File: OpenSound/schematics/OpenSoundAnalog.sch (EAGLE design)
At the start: 68 parts, among them IC1 MCP4822-E/PSOIC8, IC2 QUAD_OPAMPD, IC3 LM317MABT, Q601 BC846, Q701 BC846, Q801 BC846, Q903 BC846, U1 SN74LVC3G17DCTR

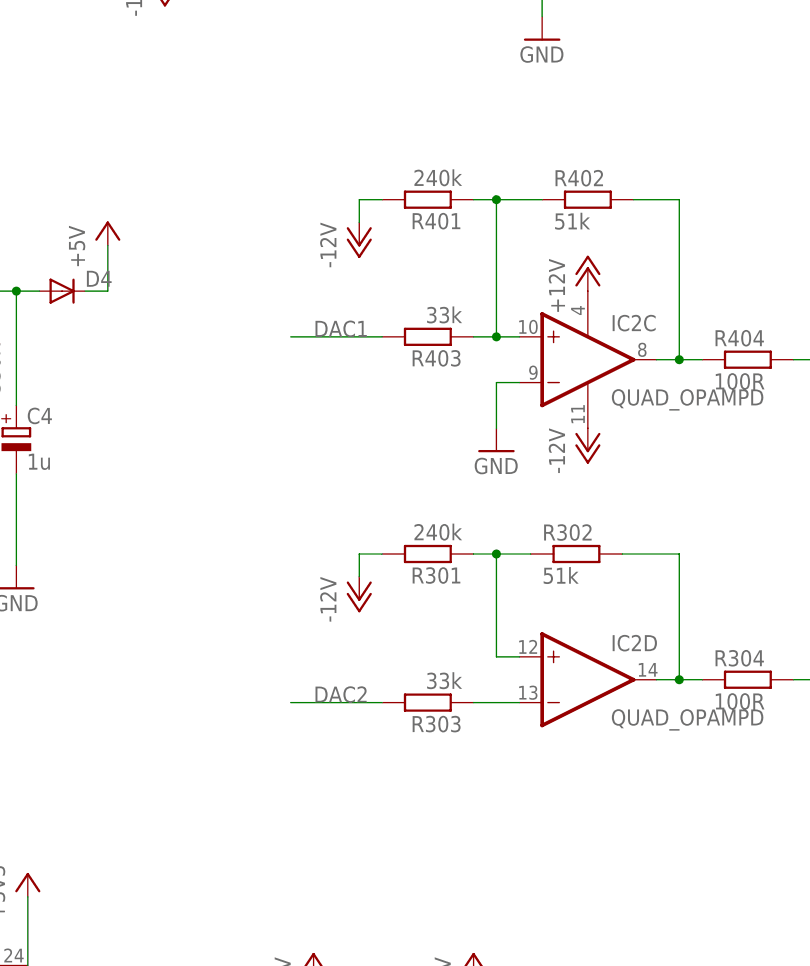
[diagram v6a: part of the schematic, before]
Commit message: fixed schmitt-trigger amps
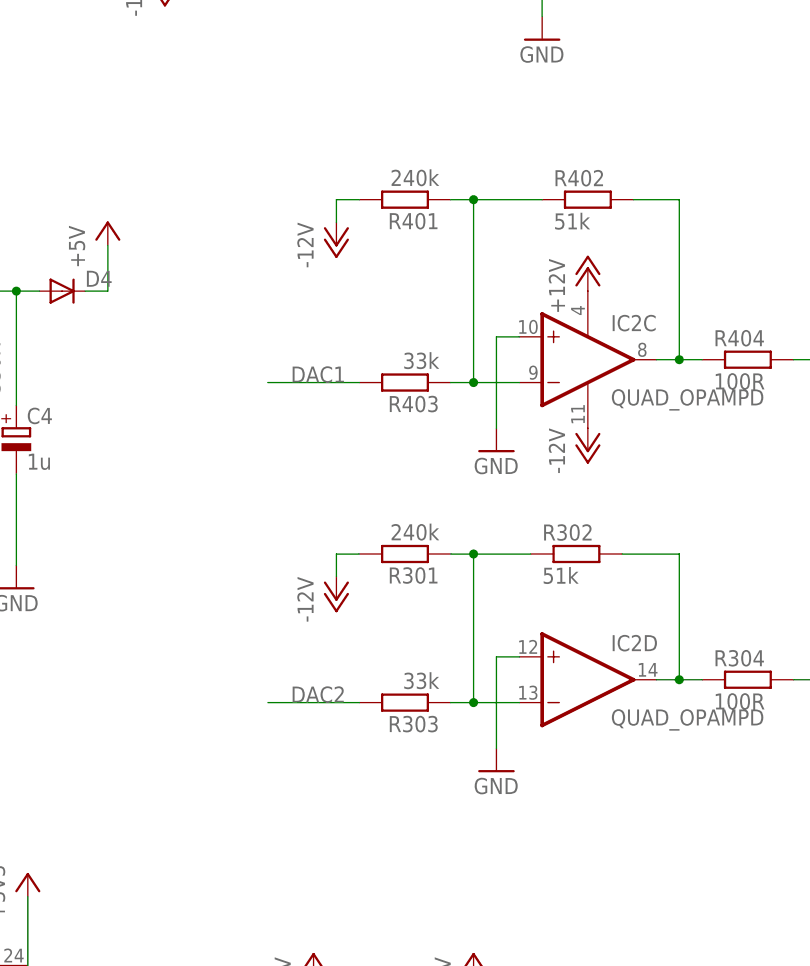
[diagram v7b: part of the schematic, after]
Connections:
- removed net N$12: IC2D.+IN, R301.1, R302.1
- net GND: now also IC2C.+IN, IC2D.+IN; no longer IC2C.-IN
- net N$13: now also IC2C.-IN; no longer IC2C.+IN
- net N$15: now also R301.1, R302.1
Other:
- moved on the sheet: R301, R303, R401, R403
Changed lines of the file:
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@@
 <part name="P+10" library="supply1" deviceset="+5V" device=""/>
 <part name="GND27" library="supply1" deviceset="GND" device=""/>
+<part name="GND1" library="supply1" deviceset="GND" device=""/>
 </parts>
 <sheets>
@@
 <instance part="TI2" gate="G$1" x="-34.29" y="-67.31" rot="R180"/>
 <instance part="CVO1" gate="G$1" x="198.12" y="38.1"/>
-<instance part="R401" gate="G$1" x="139.7" y="58.42" rot="R180"/>
+<instance part="R401" gate="G$1" x="137.16" y="58.42" rot="R180"/>
 <instance part="R402" gate="G$1" x="157.48" y="58.42"/>
 <instance part="GND6" gate="1" x="190.5" y="30.48"/>
@@
 <instance part="TO2" gate="G$1" x="19.05" y="31.75"/>
 <instance part="P+7" gate="1" x="-16.51" y="67.31"/>
-<instance part="P-6" gate="1" x="132.08" y="53.34"/>
-<instance part="GND8" gate="1" x="147.32" y="30.48"/>
-<instance part="R403" gate="G$1" x="139.7" y="43.18" rot="R180"/>
+<instance part="P-6" gate="1" x="129.54" y="53.34"/>
+<instance part="GND8" gate="1" x="147.32" y="-5.08"/>
+<instance part="R403" gate="G$1" x="137.16" y="38.1" rot="R180"/>
 <instance part="R304" gate="G$1" x="175.26" y="5.08"/>
 <instance part="CVO2" gate="G$1" x="198.12" y="2.54"/>
@@
 <instance part="GND18" gate="1" x="144.78" y="-62.23"/>
 <instance part="R302" gate="G$1" x="156.21" y="19.05"/>
-<instance part="R301" gate="G$1" x="139.7" y="19.05" rot="R180"/>
-<instance part="R303" gate="G$1" x="139.7" y="2.54" rot="R180"/>
-<instance part="P-4" gate="1" x="132.08" y="13.97"/>
+<instance part="R301" gate="G$1" x="137.16" y="19.05" rot="R180"/>
+<instance part="R303" gate="G$1" x="137.16" y="2.54" rot="R180"/>
+<instance part="P-4" gate="1" x="129.54" y="13.97"/>
 <instance part="IC3" gate="G$1" x="73.66" y="48.26"/>
 <instance part="R2" gate="G$1" x="73.66" y="25.4" rot="R90"/>
@@
 <instance part="P+10" gate="1" x="48.26" y="101.6"/>
 <instance part="GND27" gate="1" x="48.26" y="81.28"/>
+<instance part="GND1" gate="1" x="147.32" y="30.48"/>
 </instances>
 <busses>
@@
 </segment>
 <segment>
-<pinref part="GND8" gate="1" pin="GND"/>
-<wire x1="149.86" y1="38.1" x2="147.32" y2="38.1" width="0.1524" layer="91"/>
-<wire x1="147.32" y1="38.1" x2="147.32" y2="33.02" width="0.1524" layer="91"/>
-<pinref part="IC2" gate="C" pin="-IN"/>
-</segment>
-<segment>
 <pinref part="CVO2" gate="G$1" pin="5"/>
 <pinref part="GND39" gate="1" pin="GND"/>
@@
 <wire x1="48.26" y1="83.82" x2="48.26" y2="86.36" width="0.1524" layer="91"/>
 </segment>
+<segment>
+<pinref part="GND8" gate="1" pin="GND"/>
+<pinref part="IC2" gate="D" pin="+IN"/>
+<wire x1="147.32" y1="7.62" x2="147.32" y2="-2.54" width="0.1524" layer="91"/>
+<wire x1="149.86" y1="7.62" x2="147.32" y2="7.62" width="0.1524" layer="91"/>
+</segment>
+<segment>
+<pinref part="IC2" gate="C" pin="+IN"/>
+<wire x1="149.86" y1="43.18" x2="147.32" y2="43.18" width="0.1524" layer="91"/>
+<pinref part="GND1" gate="1" pin="GND"/>
+<wire x1="147.32" y1="43.18" x2="147.32" y2="33.02" width="0.1524" layer="91"/>
+</segment>
 </net>
 <net name="-12V" class="0">
@@
 <pinref part="R401" gate="G$1" pin="2"/>
 <pinref part="P-6" gate="1" pin="-12V"/>
-<wire x1="134.62" y1="58.42" x2="132.08" y2="58.42" width="0.1524" layer="91"/>
-<wire x1="132.08" y1="58.42" x2="132.08" y2="55.88" width="0.1524" layer="91"/>
+<wire x1="132.08" y1="58.42" x2="129.54" y2="58.42" width="0.1524" layer="91"/>
+<wire x1="129.54" y1="58.42" x2="129.54" y2="55.88" width="0.1524" layer="91"/>
 </segment>
 <segment>
@@
 <pinref part="R301" gate="G$1" pin="2"/>
 <pinref part="P-4" gate="1" pin="-12V"/>
-<wire x1="134.62" y1="19.05" x2="132.08" y2="19.05" width="0.1524" layer="91"/>
-<wire x1="132.08" y1="19.05" x2="132.08" y2="16.51" width="0.1524" layer="91"/>
+<wire x1="132.08" y1="19.05" x2="129.54" y2="19.05" width="0.1524" layer="91"/>
+<wire x1="129.54" y1="19.05" x2="129.54" y2="16.51" width="0.1524" layer="91"/>
 </segment>
 </net>
@@
 <segment>
 <pinref part="R403" gate="G$1" pin="1"/>
-<wire x1="149.86" y1="43.18" x2="147.32" y2="43.18" width="0.1524" layer="91"/>
 <pinref part="R401" gate="G$1" pin="1"/>
 <pinref part="R402" gate="G$1" pin="1"/>
-<wire x1="147.32" y1="43.18" x2="144.78" y2="43.18" width="0.1524" layer="91"/>
-<wire x1="144.78" y1="58.42" x2="147.32" y2="58.42" width="0.1524" layer="91"/>
-<wire x1="147.32" y1="58.42" x2="152.4" y2="58.42" width="0.1524" layer="91"/>
-<wire x1="147.32" y1="43.18" x2="147.32" y2="58.42" width="0.1524" layer="91"/>
-<junction x="147.32" y="43.18"/>
-<junction x="147.32" y="58.42"/>
-<pinref part="IC2" gate="C" pin="+IN"/>
+<wire x1="144.78" y1="38.1" x2="142.24" y2="38.1" width="0.1524" layer="91"/>
+<wire x1="142.24" y1="58.42" x2="144.78" y2="58.42" width="0.1524" layer="91"/>
+<wire x1="144.78" y1="58.42" x2="152.4" y2="58.42" width="0.1524" layer="91"/>
+<wire x1="144.78" y1="38.1" x2="144.78" y2="58.42" width="0.1524" layer="91"/>
+<junction x="144.78" y="58.42"/>
+<pinref part="IC2" gate="C" pin="-IN"/>
+<wire x1="149.86" y1="38.1" x2="144.78" y2="38.1" width="0.1524" layer="91"/>
+<junction x="144.78" y="38.1"/>
 </segment>
 </net>
@@
 <segment>
 <pinref part="R403" gate="G$1" pin="2"/>
-<wire x1="124.46" y1="43.18" x2="134.62" y2="43.18" width="0.1524" layer="91"/>
-<label x="127" y="43.18" size="1.778" layer="95"/>
+<wire x1="121.92" y1="38.1" x2="132.08" y2="38.1" width="0.1524" layer="91"/>
+<label x="124.46" y="38.1" size="1.778" layer="95"/>
 </segment>
 <segment>
@@
 <net name="DAC2" class="0">
 <segment>
-<label x="127" y="2.54" size="1.778" layer="95"/>
-<wire x1="124.46" y1="2.54" x2="134.62" y2="2.54" width="0.1524" layer="91"/>
+<label x="124.46" y="2.54" size="1.778" layer="95"/>
+<wire x1="121.92" y1="2.54" x2="132.08" y2="2.54" width="0.1524" layer="91"/>
 <pinref part="R303" gate="G$1" pin="2"/>
 </segment>
@@
 </segment>
 </net>
-<net name="N$12" class="0">
-<segment>
-<pinref part="IC2" gate="D" pin="+IN"/>
+<net name="N$15" class="0">
+<segment>
+<pinref part="IC2" gate="D" pin="-IN"/>
+<pinref part="R303" gate="G$1" pin="1"/>
+<wire x1="142.24" y1="2.54" x2="144.78" y2="2.54" width="0.1524" layer="91"/>
 <pinref part="R301" gate="G$1" pin="1"/>
 <pinref part="R302" gate="G$1" pin="1"/>
-<wire x1="151.13" y1="19.05" x2="147.32" y2="19.05" width="0.1524" layer="91"/>
-<wire x1="147.32" y1="19.05" x2="144.78" y2="19.05" width="0.1524" layer="91"/>
-<junction x="147.32" y="19.05"/>
-<wire x1="147.32" y1="19.05" x2="147.32" y2="7.62" width="0.1524" layer="91"/>
-<wire x1="147.32" y1="7.62" x2="149.86" y2="7.62" width="0.1524" layer="91"/>
-</segment>
-</net>
-<net name="N$15" class="0">
-<segment>
-<pinref part="IC2" gate="D" pin="-IN"/>
-<pinref part="R303" gate="G$1" pin="1"/>
 <wire x1="144.78" y1="2.54" x2="149.86" y2="2.54" width="0.1524" layer="91"/>
-</segment>
-</net>
+<wire x1="151.13" y1="19.05" x2="144.78" y2="19.05" width="0.1524" layer="91"/>
+<wire x1="144.78" y1="19.05" x2="142.24" y2="19.05" width="0.1524" layer="91"/>
+<junction x="144.78" y="19.05"/>
+<wire x1="144.78" y1="19.05" x2="144.78" y2="2.54" width="0.1524" layer="91"/>
+<junction x="144.78" y="2.54"/>
+</segment>
+</net>

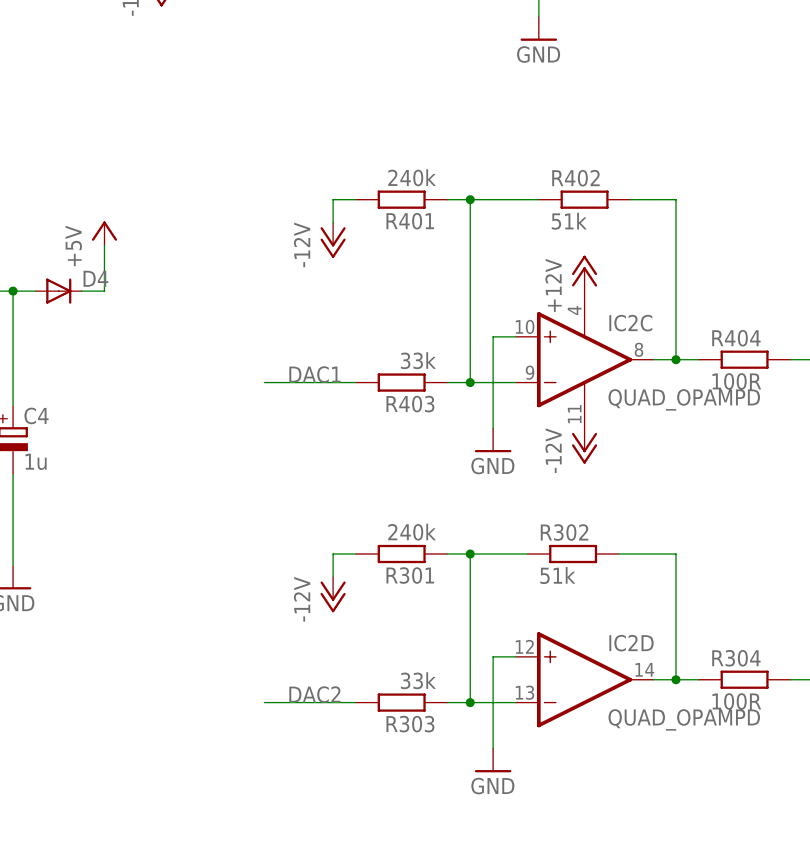
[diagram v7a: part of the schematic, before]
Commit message: changed resistor values for +-5v full scale output
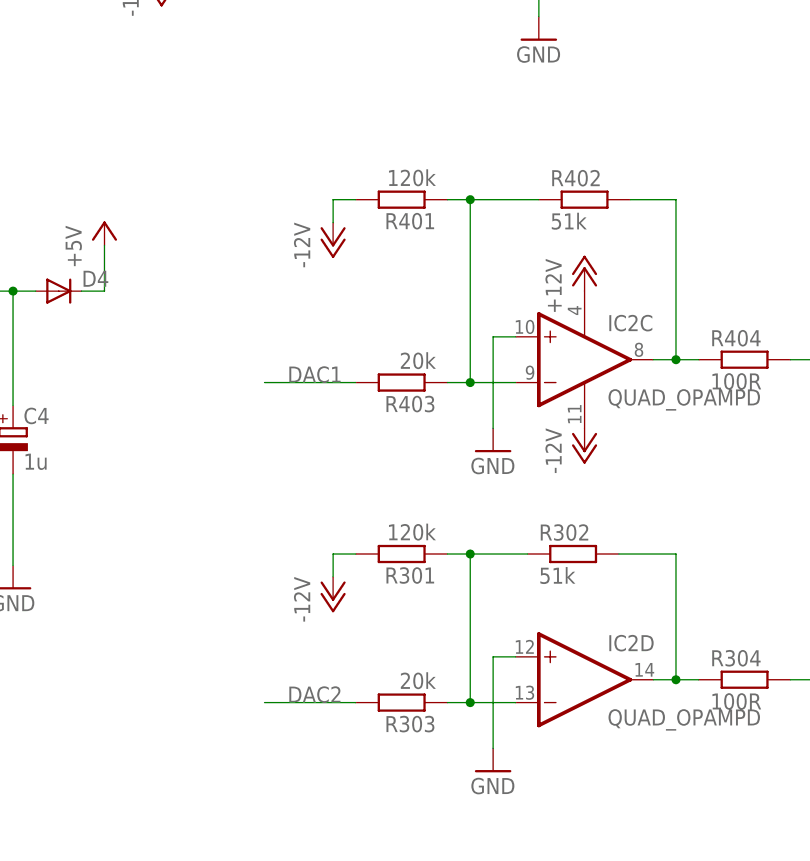
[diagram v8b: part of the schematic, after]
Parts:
- R301, R401: value 240k -> 120k
- R303, R403: value 33k -> 20k
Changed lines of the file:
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@@
 <part name="TI2" library="Rebel" deviceset="THONKICONN" device=""/>
 <part name="CVO1" library="Rebel" deviceset="THONKICONN" device=""/>
-<part name="R401" library="Rebel" deviceset="R-EU_" device="0603" value="240k"/>
+<part name="R401" library="Rebel" deviceset="R-EU_" device="0603" value="120k"/>
 <part name="R402" library="Rebel" deviceset="R-EU_" device="0603" value="51k"/>
 <part name="GND6" library="supply1" deviceset="GND" device=""/>
@@
 <part name="P-6" library="supply1" deviceset="-12V" device=""/>
 <part name="GND8" library="supply1" deviceset="GND" device=""/>
-<part name="R403" library="Rebel" deviceset="R-EU_" device="0603" value="33k"/>
+<part name="R403" library="Rebel" deviceset="R-EU_" device="0603" value="20k"/>
 <part name="R304" library="Rebel" deviceset="R-EU_" device="0603" value="100R"/>
 <part name="CVO2" library="Rebel" deviceset="THONKICONN" device=""/>
@@
 <part name="GND18" library="supply1" deviceset="GND" device=""/>
 <part name="R302" library="Rebel" deviceset="R-EU_" device="0603" value="51k"/>
-<part name="R301" library="Rebel" deviceset="R-EU_" device="0603" value="240k"/>
-<part name="R303" library="Rebel" deviceset="R-EU_" device="0603" value="33k"/>
+<part name="R301" library="Rebel" deviceset="R-EU_" device="0603" value="120k"/>
+<part name="R303" library="Rebel" deviceset="R-EU_" device="0603" value="20k"/>
 <part name="P-4" library="supply1" deviceset="-12V" device=""/>
 <part name="IC3" library="v-reg" deviceset="LM317?*" device="MABT"/>
